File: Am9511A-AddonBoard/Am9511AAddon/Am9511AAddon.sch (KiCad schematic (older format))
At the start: 16 parts, among them J1 Conn_02x12, J2 Conn_01x02, U1 MCP810, U2 74HCT573, U3 74HCT574, U4 74HCT00, U5 XTAL OSC 3.0 MHz, U6 Am9511A-1DC

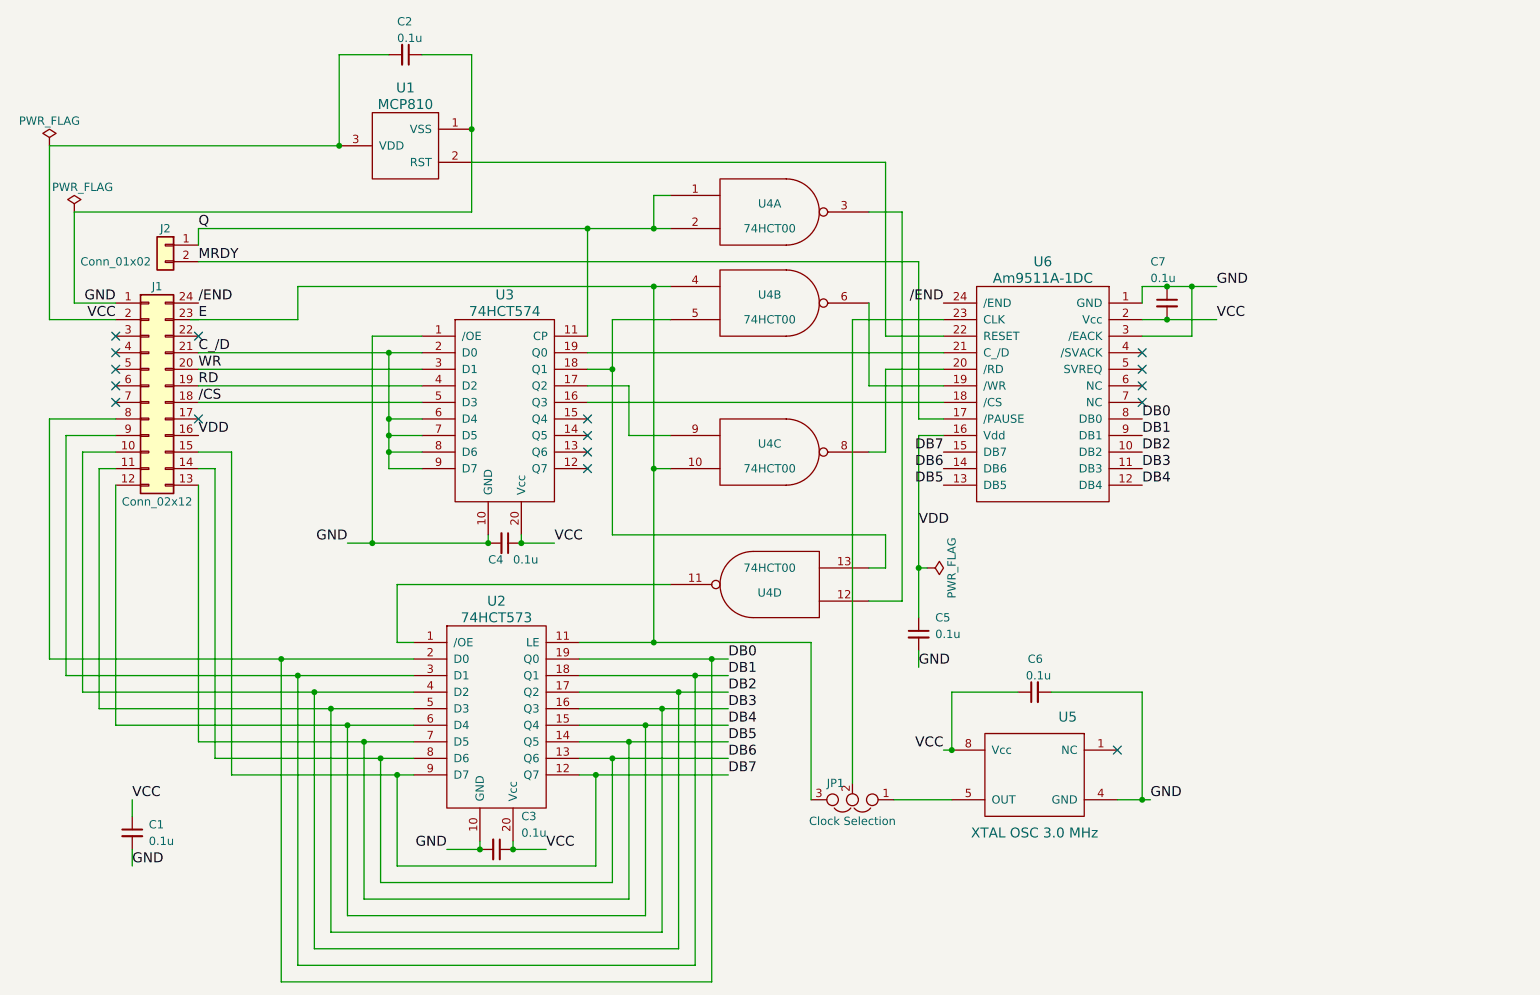
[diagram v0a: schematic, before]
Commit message: Update design materials of Am9511A Add-on board (now, Rev.2)
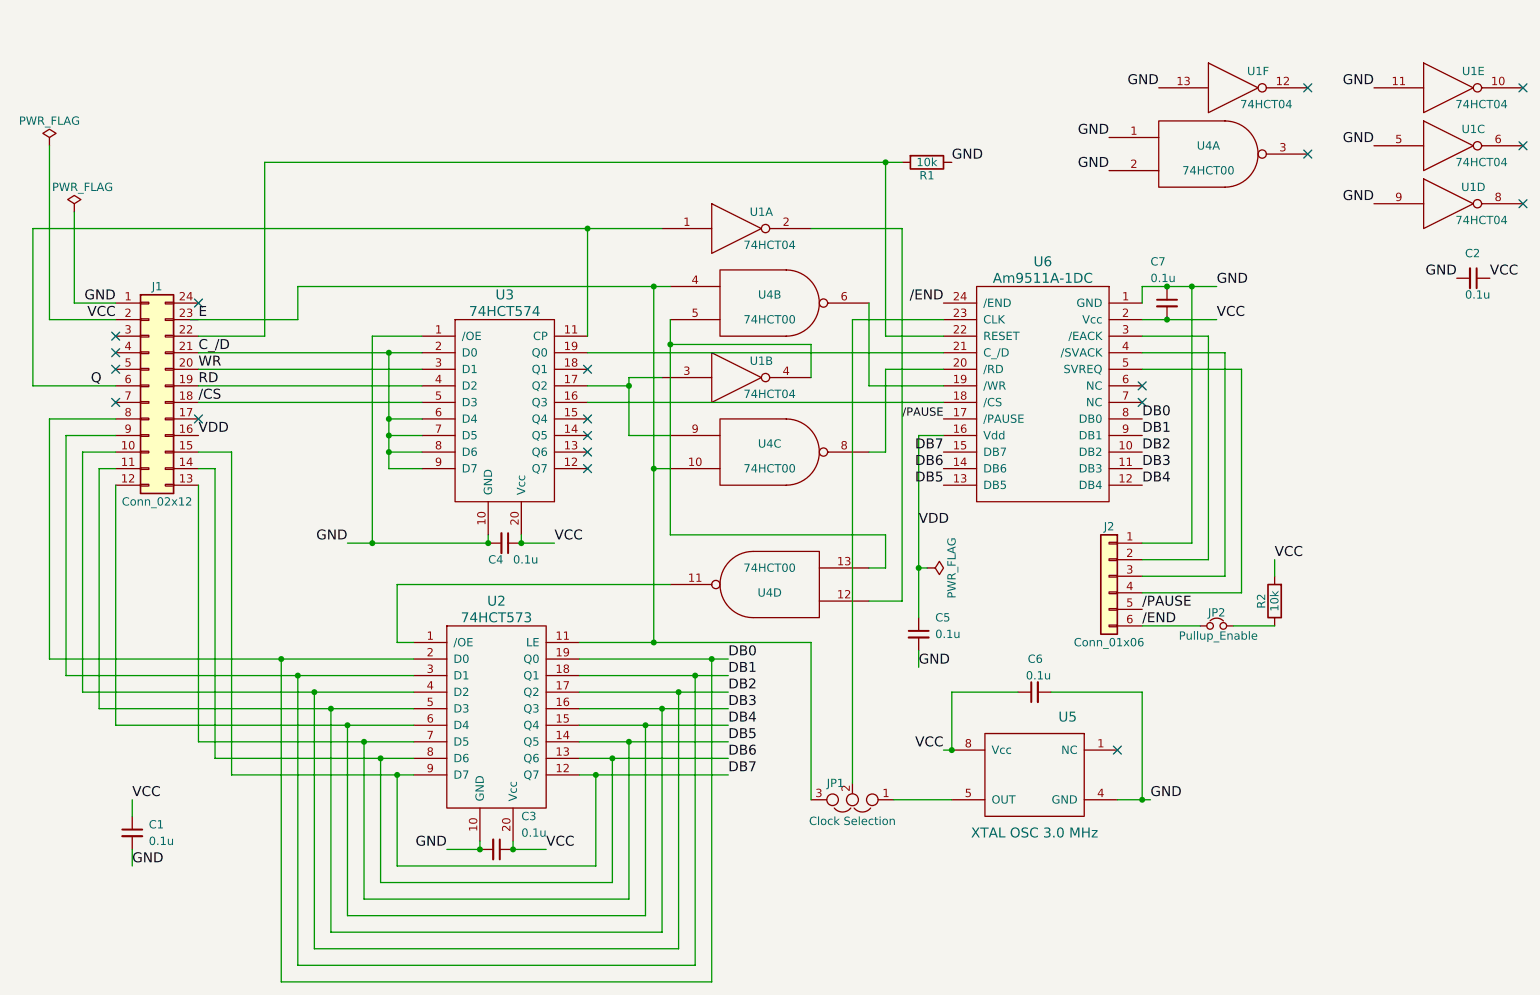
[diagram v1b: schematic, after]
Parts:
- removed J2: Conn_01x02, Pin_Headers:Pin_Header_Angled_1x02_Pitch2.54mm, symbol Conn_01x02
- removed U1: MCP810, TO_SOT_Packages_SMD:SOT-23, symbol MCP810
- added J2: Conn_01x06, Pin_Headers:Pin_Header_Straight_1x06_Pitch2.54mm, symbol Conn_01x06
- added JP2: Pullup_Enable, Pin_Headers:Pin_Header_Straight_1x02_Pitch2.54mm, symbol Jumper_NC_Small
- added R1, R2: 10k, Resistors_THT:R_Axial_DIN0207_L6.3mm_D2.5mm_P10.16mm_Horizontal, symbol R
- added U1: 74HCT04, Housings_DIP:DIP-14_W7.62mm, symbol 74HC04
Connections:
- net /END: now also J2.6 (Pin_6), JP2.1; no longer J1.24 (Pin_24)
- net GND: now also C2.2, U4.1, U4.2, J2.1 (Pin_1), R1.1, U1.11, U1.13, U1.5, U1.7 (GND), U1.7 (GND), U1.7 (GND), U1.7 (GND), U1.7 (GND), U1.7 (GND), U1.9; no longer C2.1, U6.3 (/EACK)
- net Q: now also J1.6 (Pin_6), U1.1; no longer U4.1, U4.2
- net VCC: now also C2.1, R2.2, U1.14 (VCC), U1.14 (VCC), U1.14 (VCC), U1.14 (VCC), U1.14 (VCC), U1.14 (VCC); no longer C2.2
- net at J1.22 (Pin_22): now also U6.22 (RESET), R1.2
- net at U3.17 (Q2), U4.9: now also U1.3
- net at U4.13, U4.5: now also U1.4; no longer U3.18 (Q1)
- net at U4.12: now also U1.2; no longer U4.3
- net at U6.4 (/SVACK): now also J2.3 (Pin_3)
- net at U6.5 (SVREQ): now also J2.4 (Pin_4)
- net MRDY renamed /PAUSE
- net /PAUSE: now also J2.5 (Pin_5)
- new net: J2.2 (Pin_2), U6.3 (/EACK)
- new net: JP2.2, R2.1
- no-connect marks 16 -> 19
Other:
- moved on the sheet: C2, U4A
